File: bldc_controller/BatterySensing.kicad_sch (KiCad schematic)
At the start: 3 parts

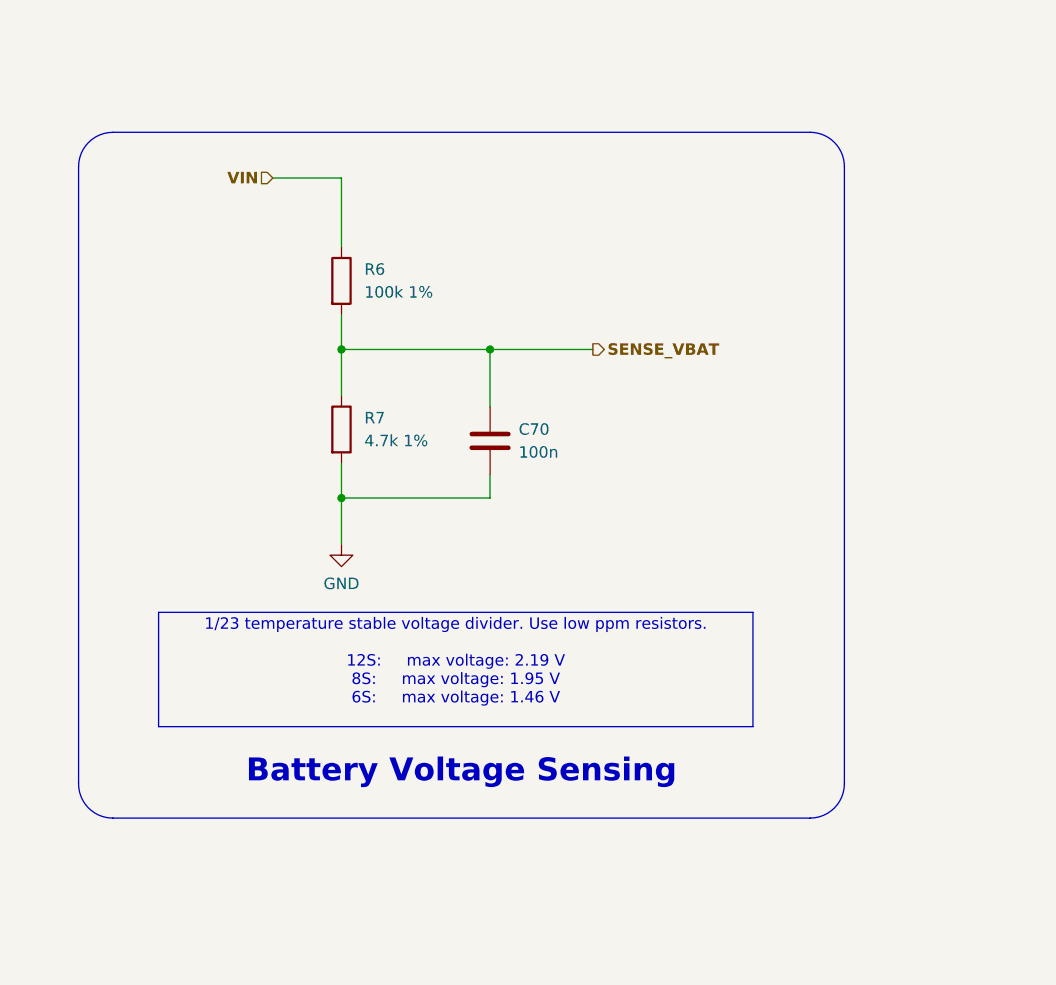
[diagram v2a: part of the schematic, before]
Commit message: Added TVS diodes to all interfaces
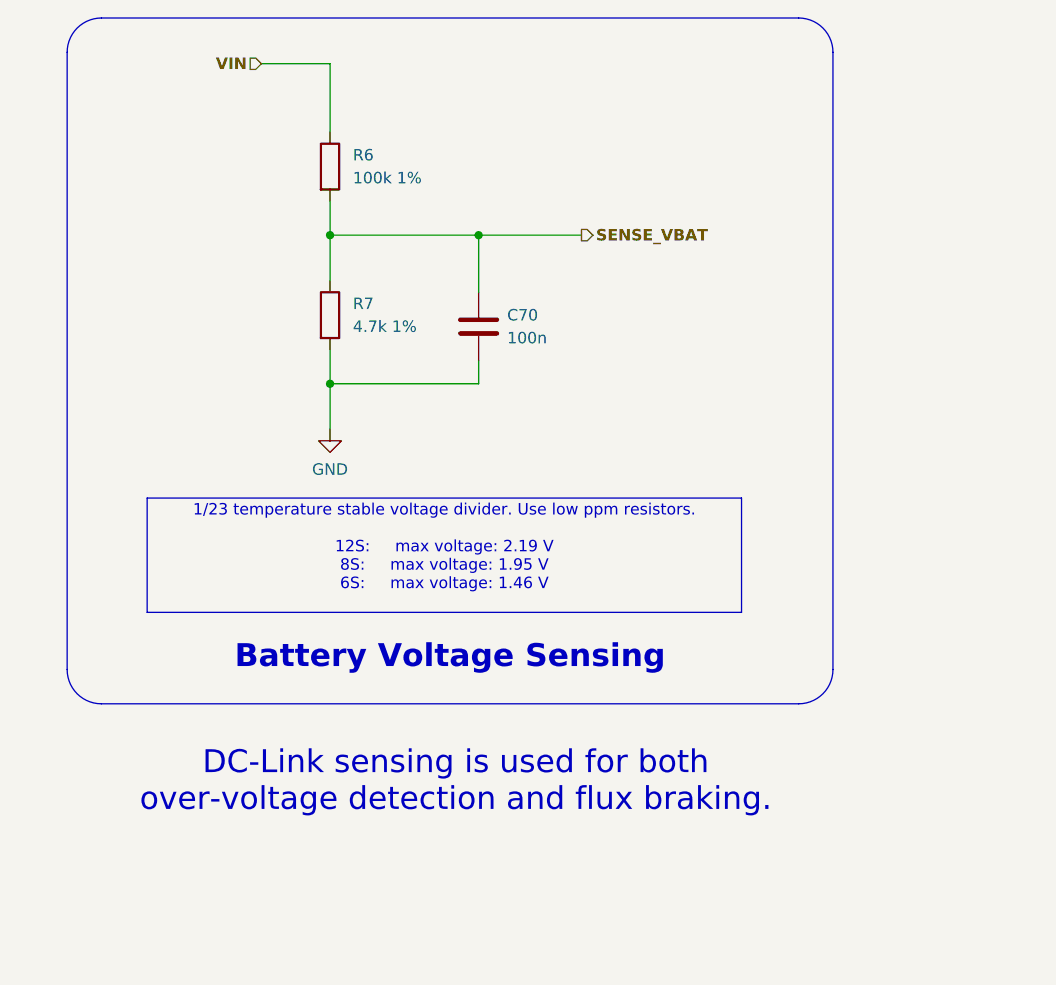
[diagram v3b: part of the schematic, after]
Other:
- moved on the sheet: C70, R6, R7
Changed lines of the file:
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@@
     (comment 3 "Author: Vincent Nguyen")
   )
-  (junction (at 147.32 83.82) (diameter 0) (color 0 0 0 0)
+  (junction (at 146.05 71.12) (diameter 0) (color 0 0 0 0)
   )
-  (junction (at 163.83 83.82) (diameter 0) (color 0 0 0 0)
+  (junction (at 162.56 71.12) (diameter 0) (color 0 0 0 0)
   )
-  (junction (at 147.32 100.33) (diameter 0) (color 0 0 0 0)
+  (junction (at 146.05 87.63) (diameter 0) (color 0 0 0 0)
   )
-  (polyline (pts (xy 118.11 63.5) (xy 118.11 132.08))
+  (polyline (pts (xy 116.84 50.8) (xy 116.84 119.38))
     (stroke (width 0) (type default))
   )
-  (wire (pts (xy 163.83 83.82) (xy 163.83 90.17))
+  (wire (pts (xy 162.56 71.12) (xy 162.56 77.47))
     (stroke (width 0) (type default))
   )
-  (wire (pts (xy 163.83 83.82) (xy 147.32 83.82))
+  (wire (pts (xy 162.56 71.12) (xy 146.05 71.12))
     (stroke (width 0) (type default))
   )
-  (wire (pts (xy 163.83 97.79) (xy 163.83 100.33))
+  (wire (pts (xy 162.56 85.09) (xy 162.56 87.63))
     (stroke (width 0) (type default))
   )
-  (polyline (pts (xy 203.2 63.5) (xy 203.2 132.08))
+  (polyline (pts (xy 201.93 50.8) (xy 201.93 119.38))
     (stroke (width 0) (type default))
   )
-  (polyline (pts (xy 199.39 135.89) (xy 121.92 135.89))
+  (polyline (pts (xy 198.12 123.19) (xy 120.65 123.19))
     (stroke (width 0) (type default))
   )
-  (wire (pts (xy 147.32 83.82) (xy 147.32 88.9))
+  (wire (pts (xy 146.05 71.12) (xy 146.05 76.2))
     (stroke (width 0) (type default))
   )
-  (wire (pts (xy 163.83 100.33) (xy 147.32 100.33))
+  (wire (pts (xy 162.56 87.63) (xy 146.05 87.63))
     (stroke (width 0) (type default))
   )
-  (wire (pts (xy 147.32 64.77) (xy 147.32 72.39))
+  (wire (pts (xy 146.05 52.07) (xy 146.05 59.69))
     (stroke (width 0.381) (type default) (color 200 50 50 1))
   )
-  (wire (pts (xy 163.83 83.82) (xy 175.26 83.82))
+  (wire (pts (xy 162.56 71.12) (xy 173.99 71.12))
     (stroke (width 0) (type default))
   )
-  (wire (pts (xy 147.32 80.01) (xy 147.32 83.82))
+  (wire (pts (xy 146.05 67.31) (xy 146.05 71.12))
     (stroke (width 0) (type default))
   )
-  (wire (pts (xy 139.7 64.77) (xy 147.32 64.77))
+  (wire (pts (xy 138.43 52.07) (xy 146.05 52.07))
     (stroke (width 0.381) (type default) (color 200 50 50 1))
   )
-  (wire (pts (xy 147.32 105.41) (xy 147.32 100.33))
+  (wire (pts (xy 146.05 92.71) (xy 146.05 87.63))
     (stroke (width 0) (type default))
   )
-  (wire (pts (xy 147.32 100.33) (xy 147.32 96.52))
+  (wire (pts (xy 146.05 87.63) (xy 146.05 83.82))
     (stroke (width 0) (type default))
   )
-  (polyline (pts (xy 121.92 59.69) (xy 199.39 59.69))
+  (polyline (pts (xy 120.65 46.99) (xy 198.12 46.99))
     (stroke (width 0) (type default))
   )
-  (arc (start 199.39 59.69) (mid 202.0838 60.8048) (end 203.2 63.5)
+  (arc (start 198.12 46.99) (mid 200.8141 48.1059) (end 201.93 50.8)
     (stroke (width 0) (type default))
     (fill (type none))
   )
-  (arc (start 203.2 132.08) (mid 202.0838 134.7723) (end 199.39 135.89)
+  (arc (start 201.93 119.38) (mid 200.8141 122.0741) (end 198.12 123.19)
     (stroke (width 0) (type default))
     (fill (type none))
   )
-  (arc (start 121.92 135.89) (mid 119.2227 134.7758) (end 118.11 132.08)
+  (arc (start 120.65 123.19) (mid 117.953 122.077) (end 116.84 119.38)
     (stroke (width 0) (type default))
     (fill (type none))
   )
-  (arc (start 118.11 63.5) (mid 119.2262 60.8077) (end 121.92 59.69)
+  (arc (start 116.84 50.8) (mid 117.9559 48.1059) (end 120.65 46.99)
     (stroke (width 0) (type default))
     (fill (type none))
@@
     (effects (font (size 2.54 2.54) (thickness 0.508) bold (color 0 0 0 1)) (href "#1"))
   )
+  (text_box "DC-Link sensing is used for both over-voltage detection and flux braking."
+    (at 118.11 125.73 0) (size 83.82 11.43)
+    (stroke (width -0.0001) (type default))
+    (fill (type none))
+    (effects (font (size 2.54 2.54) (color 0 0 0 1)) (justify bottom))
+  )
   (text_box "Battery Voltage Sensing"
-    (at 120.015 124.46 0) (size 81.28 9.525)
+    (at 118.745 111.76 0) (size 81.28 9.525)
     (stroke (width -0.0001) (type default))
     (fill (type none))
@@
   )
   (text_box "1/23 temperature stable voltage divider. Use low ppm resistors.\n\n12S: 	max voltage: 2.19 V\n8S: 	max voltage: 1.95 V\n6S: 	max voltage: 1.46 V\n\n"
-    (at 127 113.03 0) (size 66.04 12.7)
+    (at 125.73 100.33 0) (size 66.04 12.7)
     (stroke (width 0) (type default) (color 0 0 0 1))
     (fill (type color) (color 191 240 255 1))
     (effects (font (size 1.27 1.27) (color 0 0 0 1)))
   )
-  (hierarchical_label "VIN" (shape input) (at 139.7 64.77 180) (fields_autoplaced)
+  (hierarchical_label "VIN" (shape input) (at 138.43 52.07 180) (fields_autoplaced)
     (effects (font (size 1.27 1.27) bold) (justify right))
   )
-  (hierarchical_label "SENSE_VBAT" (shape output) (at 175.26 83.82 0) (fields_autoplaced)
+  (hierarchical_label "SENSE_VBAT" (shape output) (at 173.99 71.12 0) (fields_autoplaced)
     (effects (font (size 1.27 1.27) bold) (justify left))
   )
-  (symbol (lib_id "Device:R") (at 147.32 92.71 0) (unit 1)
+  (symbol (lib_id "Device:R") (at 146.05 80.01 0) (unit 1)
     (in_bom yes) (on_board yes) (dnp no) (fields_autoplaced)
-    (property "Reference" "R7" (at 149.86 91.44 0)
+    (property "Reference" "R7" (at 148.59 78.74 0)
       (effects (font (size 1.27 1.27)) (justify left))
     )
-    (property "Value" "4.7k 1%" (at 149.86 93.98 0)
+    (property "Value" "4.7k 1%" (at 148.59 81.28 0)
       (effects (font (size 1.27 1.27)) (justify left))
     )
-    (property "Footprint" "0_resistor_smd:R_0402_1005_DensityHigh" (at 145.542 92.71 90)
+    (property "Footprint" "0_resistor_smd:R_0402_1005_DensityHigh" (at 144.272 80.01 90)
       (effects (font (size 1.27 1.27)) hide)
     )
-    (property "Datasheet" "~" (at 147.32 92.71 0)
+    (property "Datasheet" "~" (at 146.05 80.01 0)
       (effects (font (size 1.27 1.27)) hide)
     )
@@
     )
   )
-  (symbol (lib_id "Device:C") (at 163.83 93.98 0) (unit 1)
+  (symbol (lib_id "Device:C") (at 162.56 81.28 0) (unit 1)
     (in_bom yes) (on_board yes) (dnp no) (fields_autoplaced)
-    (property "Reference" "C70" (at 167.005 92.71 0)
+    (property "Reference" "C70" (at 165.735 80.01 0)
       (effects (font (size 1.27 1.27)) (justify left))
     )
-    (property "Value" "100n" (at 167.005 95.25 0)
+    (property "Value" "100n" (at 165.735 82.55 0)
       (effects (font (size 1.27 1.27)) (justify left))
     )
-    (property "Footprint" "0_capacitor_smd:C_0402_1005_DensityHigh" (at 164.7952 97.79 0)
+    (property "Footprint" "0_capacitor_smd:C_0402_1005_DensityHigh" (at 163.5252 85.09 0)
       (effects (font (size 1.27 1.27)) hide)
     )
-    (property "Datasheet" "~" (at 163.83 93.98 0)
+    (property "Datasheet" "~" (at 162.56 81.28 0)
       (effects (font (size 1.27 1.27)) hide)
     )
@@
     )
   )
-  (symbol (lib_id "power:GND") (at 147.32 105.41 0) (unit 1)
+  (symbol (lib_id "power:GND") (at 146.05 92.71 0) (unit 1)
     (in_bom yes) (on_board yes) (dnp no) (fields_autoplaced)
-    (property "Reference" "#PWR021" (at 147.32 111.76 0)
+    (property "Reference" "#PWR021" (at 146.05 99.06 0)
       (effects (font (size 1.27 1.27)) hide)
     )
-    (property "Value" "GND" (at 147.32 109.855 0)
+    (property "Value" "GND" (at 146.05 97.155 0)
       (effects (font (size 1.27 1.27)))
     )
-    (property "Footprint" "" (at 147.32 105.41 0)
+    (property "Footprint" "" (at 146.05 92.71 0)
       (effects (font (size 1.27 1.27)) hide)
     )
-    (property "Datasheet" "" (at 147.32 105.41 0)
+    (property "Datasheet" "" (at 146.05 92.71 0)
       (effects (font (size 1.27 1.27)) hide)
     )
@@
     )
   )
-  (symbol (lib_id "Device:R") (at 147.32 76.2 0) (unit 1)
+  (symbol (lib_id "Device:R") (at 146.05 63.5 0) (unit 1)
     (in_bom yes) (on_board yes) (dnp no) (fields_autoplaced)
-    (property "Reference" "R6" (at 149.86 74.93 0)
+    (property "Reference" "R6" (at 148.59 62.23 0)
       (effects (font (size 1.27 1.27)) (justify left))
     )
-    (property "Value" "100k 1%" (at 149.86 77.47 0)
+    (property "Value" "100k 1%" (at 148.59 64.77 0)
       (effects (font (size 1.27 1.27)) (justify left))
     )
-    (property "Footprint" "0_resistor_smd:R_0402_1005_DensityHigh" (at 145.542 76.2 90)
+    (property "Footprint" "0_resistor_smd:R_0402_1005_DensityHigh" (at 144.272 63.5 90)
       (effects (font (size 1.27 1.27)) hide)
     )
-    (property "Datasheet" "~" (at 147.32 76.2 0)
+    (property "Datasheet" "~" (at 146.05 63.5 0)
       (effects (font (size 1.27 1.27)) hide)
     )

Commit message: might have fixed net issue, added dxf and svgs
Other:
- moved on the sheet: C70, R6, R7

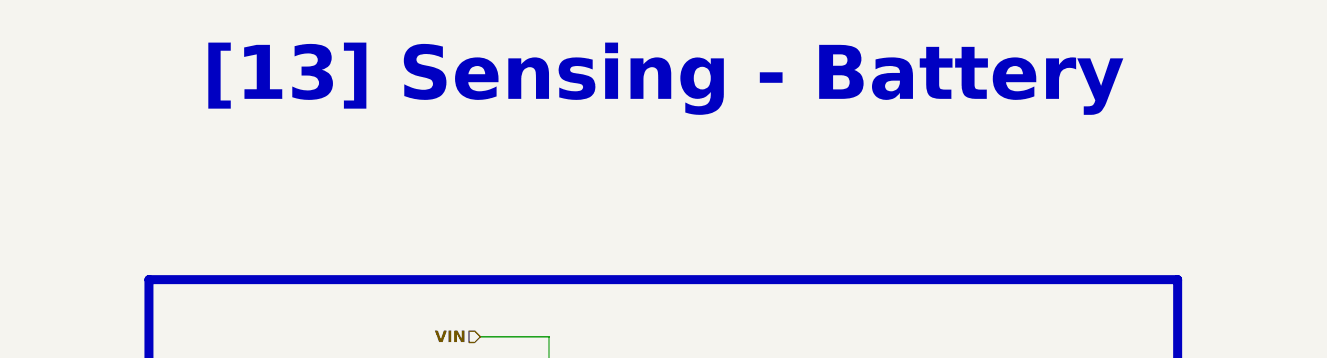
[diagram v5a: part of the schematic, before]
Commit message: Replaced 3v3 buck with WSON package alternative. Will back-annotate components
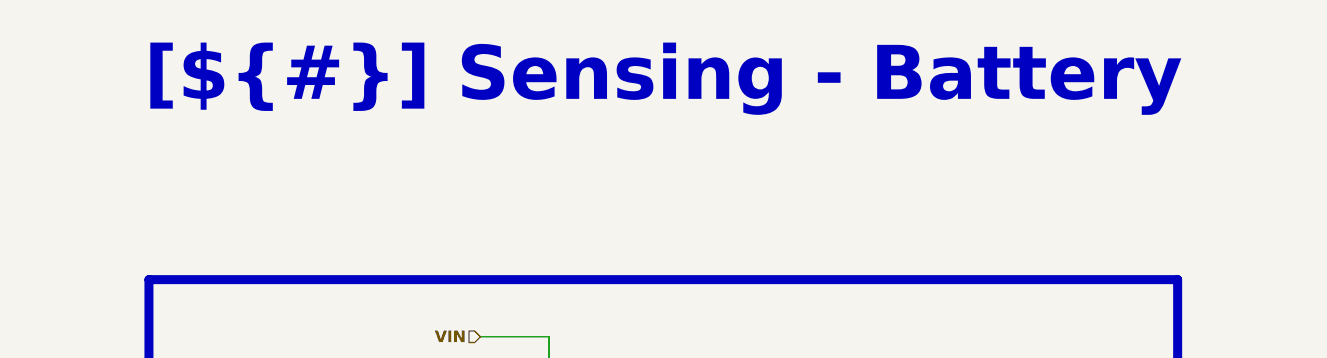
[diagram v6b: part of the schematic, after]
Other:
- company: EPFL Xplore -> ${COMPANY}
- title: Battery Sensing Voltage Divider -> Sensing - Battery
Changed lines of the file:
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@@
   (paper "A4")
   (title_block
-    (title "Battery Sensing Voltage Divider")
+    (title "Sensing - Battery")
     (date "2023-10-14")
-    (rev "1.0")
-    (company "EPFL Xplore")
-    (comment 3 "Author: Vincent Nguyen")
+    (rev "${REVISION}")
+    (company "${COMPANY}")
+    (comment 3 "Author: ${AUTHOR}")
   )
   (junction (at 134.62 71.12) (diameter 0) (color 0 0 0 0)
@@
   (junction (at 151.13 71.12) (diameter 0) (color 0 0 0 0)
   )
-  (junction (at 134.62 87.63) (diameter 0) (color 0 0 0 1)
+  (junction (at 134.62 87.63) (diameter 0) (color 0 0 0 0)
   )
   (wire (pts (xy 151.13 71.12) (xy 151.13 77.47))
@@
   )
   (wire (pts (xy 151.13 85.09) (xy 151.13 87.63))
-    (stroke (width 0.381) (type default) (color 0 0 0 1))
+    (stroke (width 0) (type default))
   )
   (wire (pts (xy 134.62 71.12) (xy 134.62 76.2))
@@
   )
   (wire (pts (xy 151.13 87.63) (xy 134.62 87.63))
-    (stroke (width 0.381) (type default) (color 0 0 0 1))
+    (stroke (width 0) (type default))
   )
   (wire (pts (xy 134.62 52.07) (xy 134.62 59.69))
@@
   )
   (wire (pts (xy 134.62 92.71) (xy 134.62 87.63))
-    (stroke (width 0.381) (type default) (color 0 0 0 1))
+    (stroke (width 0) (type default))
   )
   (wire (pts (xy 134.62 87.63) (xy 134.62 83.82))
-    (stroke (width 0.381) (type default) (color 0 0 0 1))
+    (stroke (width 0) (type default))
   )
   (rectangle (start 90.17 45.72) (end 204.47 128.27)
@@
     (fill (type none))
   )
-  (text_box "[13] Sensing - Battery"
+  (text_box "[${#}] ${TITLE}"
     (at 78.74 16.51 0) (size 137.16 12.7)
     (stroke (width -0.0001) (type default))

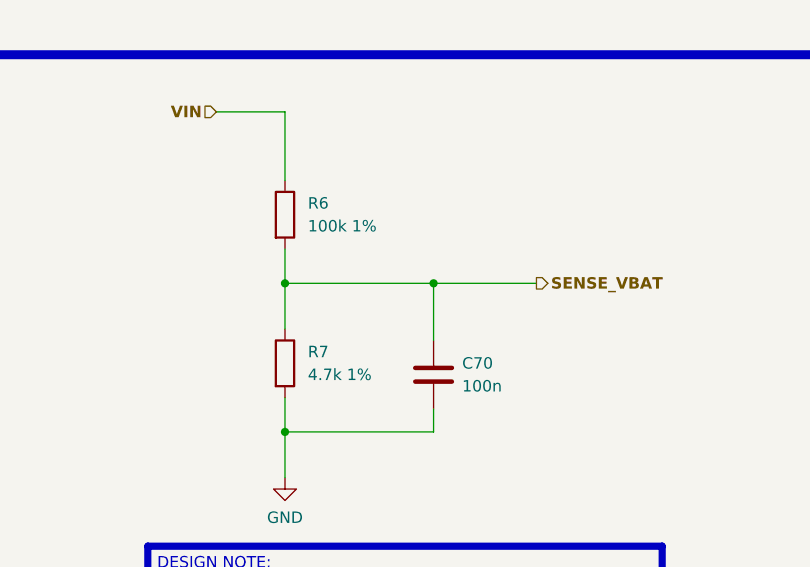
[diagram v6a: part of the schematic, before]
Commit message: routed all signals. TODO: redo all power polygons and ensure good return paths/reference. Added 3d models
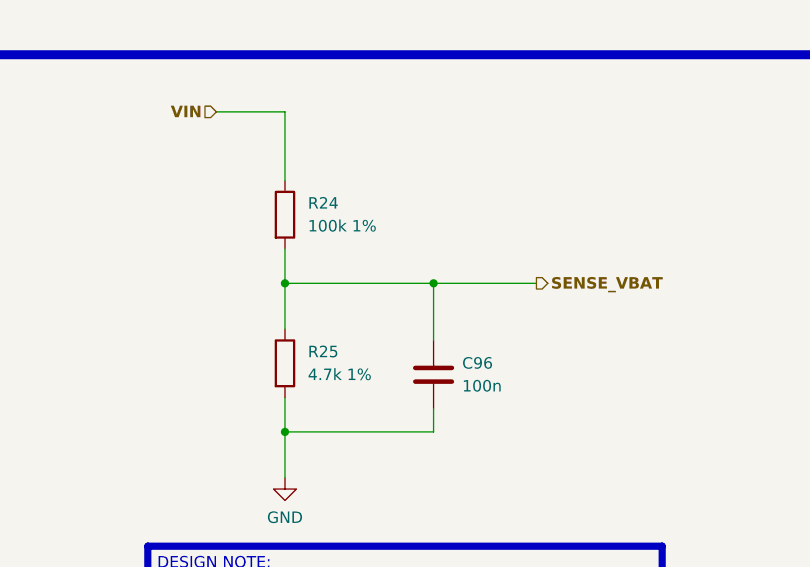
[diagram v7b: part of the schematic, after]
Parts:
- renumbered C70 to C96, R6 to R24, R7 to R25
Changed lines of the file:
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@@
   (symbol (lib_id "Device:R") (at 134.62 80.01 0) (unit 1)
     (in_bom yes) (on_board yes) (dnp no) (fields_autoplaced)
-    (property "Reference" "R7" (at 137.16 78.74 0)
+    (property "Reference" "R25" (at 137.16 78.74 0)
       (effects (font (size 1.27 1.27)) (justify left))
     )
@@
       (project "bldc_controller"
         (path "/0650c7a8-acba-429c-9f8e-eec0baf0bc1c/fede4c36-00cc-4d3d-b71c-5243ba232202/5af28e14-08f4-4265-bd51-d6e5daa4b8a2"
-          (reference "R7") (unit 1)
+          (reference "R25") (unit 1)
         )
       )
@@
   (symbol (lib_id "Device:C") (at 151.13 81.28 0) (unit 1)
     (in_bom yes) (on_board yes) (dnp no) (fields_autoplaced)
-    (property "Reference" "C70" (at 154.305 80.01 0)
+    (property "Reference" "C96" (at 154.305 80.01 0)
       (effects (font (size 1.27 1.27)) (justify left))
     )
@@
       (project "bldc_controller"
         (path "/0650c7a8-acba-429c-9f8e-eec0baf0bc1c/fede4c36-00cc-4d3d-b71c-5243ba232202/5af28e14-08f4-4265-bd51-d6e5daa4b8a2"
-          (reference "C70") (unit 1)
+          (reference "C96") (unit 1)
         )
       )
@@
   (symbol (lib_id "power:GND") (at 134.62 92.71 0) (unit 1)
     (in_bom yes) (on_board yes) (dnp no) (fields_autoplaced)
-    (property "Reference" "#PWR010" (at 134.62 99.06 0)
+    (property "Reference" "#PWR044" (at 134.62 99.06 0)
       (effects (font (size 1.27 1.27)) hide)
     )
@@
       (project "bldc_controller"
         (path "/0650c7a8-acba-429c-9f8e-eec0baf0bc1c/fede4c36-00cc-4d3d-b71c-5243ba232202/5af28e14-08f4-4265-bd51-d6e5daa4b8a2"
-          (reference "#PWR010") (unit 1)
+          (reference "#PWR044") (unit 1)
         )
       )
@@
   (symbol (lib_id "Device:R") (at 134.62 63.5 0) (unit 1)
     (in_bom yes) (on_board yes) (dnp no) (fields_autoplaced)
-    (property "Reference" "R6" (at 137.16 62.23 0)
+    (property "Reference" "R24" (at 137.16 62.23 0)
       (effects (font (size 1.27 1.27)) (justify left))
     )
@@
       (project "bldc_controller"
         (path "/0650c7a8-acba-429c-9f8e-eec0baf0bc1c/fede4c36-00cc-4d3d-b71c-5243ba232202/5af28e14-08f4-4265-bd51-d6e5daa4b8a2"
-          (reference "R6") (unit 1)
+          (reference "R24") (unit 1)
         )
       )
